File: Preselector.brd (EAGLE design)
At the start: 183 x 123.8 mm, 167 parts, among them IC4 TPS7A8101DRB, IC58 LMZ31707RVQ, Q2 FDV303N, X1 0733660061, X10 0733660061, X11 0733660061, X12 0733660061, X13 0733660061, X14 0733660061, X15 0733660061, X16 0733660061, X17 0733660061, X18 0733660061, X19 0733660061, X2 0733660061, X20 0733660061, X21 0733660061, X22 0733660061, X23 0733660061, X24 0733660061, X25 0733660061, X26 0733660061, X27 0733660061, X28 0733660061, X29 0733660061, X3 0733660061, X30 0733660061, X31 0733660061, X32 0733660061, X4 0733660061, X5 0733660061, X6 0733660061, X7 0733660061, X8 0733660061, X9 0733660061

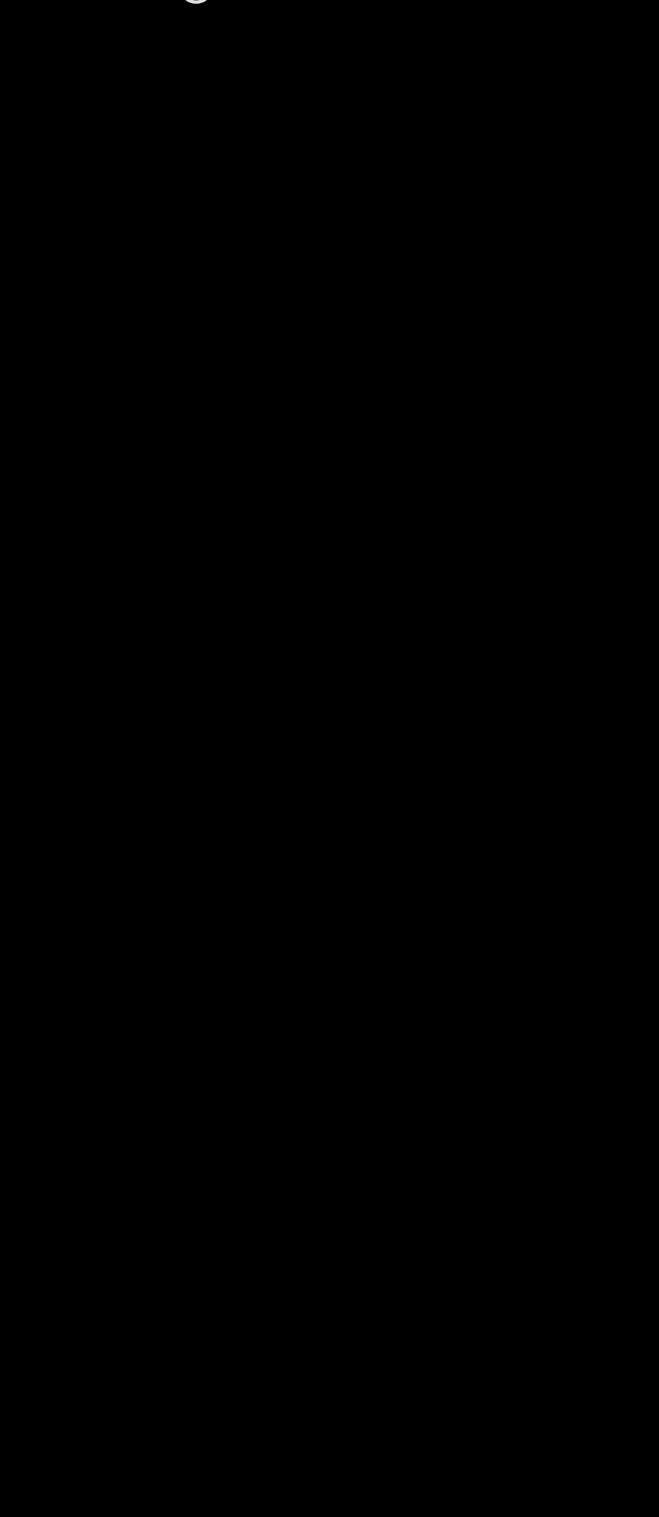
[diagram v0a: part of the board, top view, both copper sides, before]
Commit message: Added first 2 LDO's on 2m band
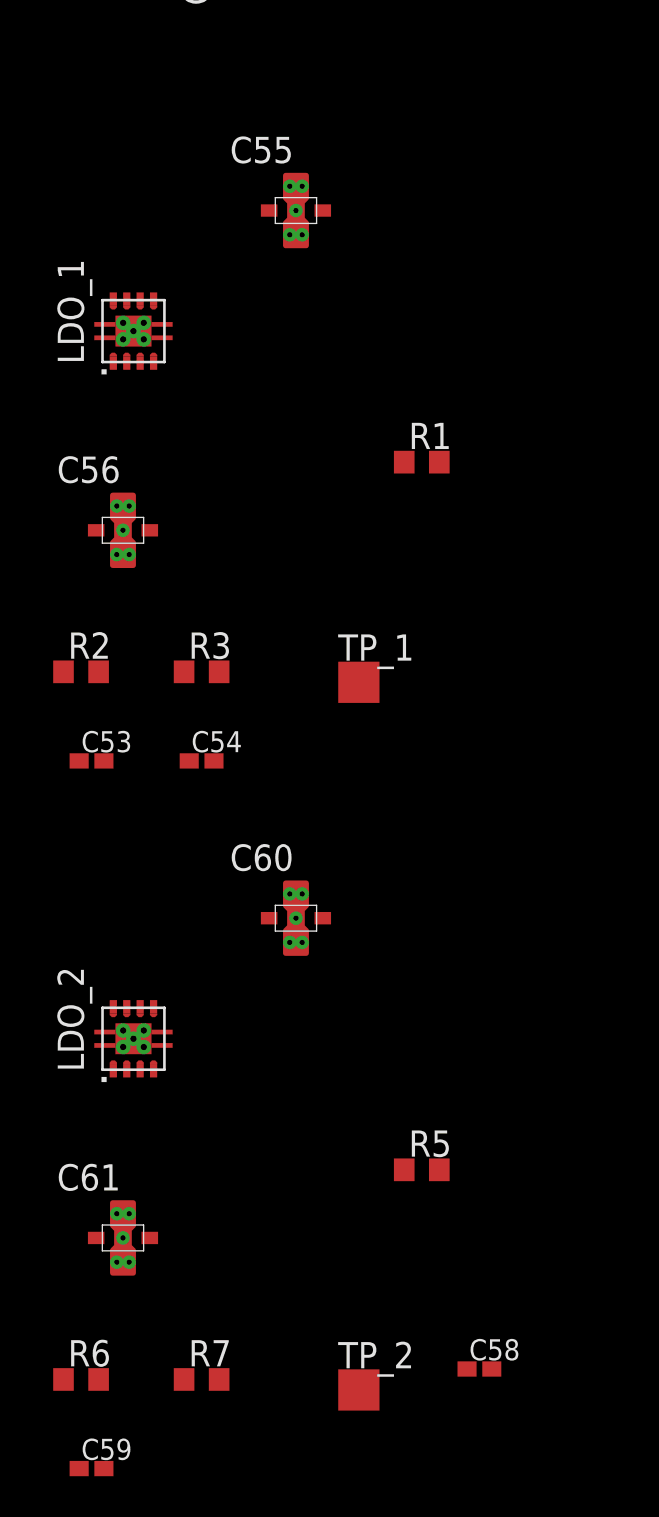
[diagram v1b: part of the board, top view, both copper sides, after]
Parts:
- added C53, C54, C58, C59: 470n, rcl:C0402K
- added C55, C56, C60, C61: NFM21PS106B0J3D, DEEP EDDY:NFM21PS
- added LDO_1, LDO_2: TPS7A8101DRB, DEEP EDDY:DRB
- added R1, R3, R5, R7: 10.0k, rcl:R0603
- added R2, R6: 52.3k, rcl:R0603
- added TP_1, TP_2: TPTP20SQ, testpad:TP20SQ
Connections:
- new net LDO_1_5V: C2.1, C3.1, C54.2, C56.OUT, L1.2, R2.1, TP_1.TP
- new net LDO_1_5V1: C59.2, C61.OUT, R6.1, TP_2.TP
- new net N$12: C54.1, LDO_1.3, R2.2, R3.1
- new net N$13: C53.1, LDO_1.6
- new net N$14: C55.OUT, LDO_1.7, LDO_1.8
- new net N$15: C56.IN, LDO_1.1, LDO_1.2
- new net N$16: C59.1, LDO_2.3, R6.2, R7.1
- new net N$17: C58.1, LDO_2.6
- new net N$18: C60.OUT, LDO_2.7, LDO_2.8
- new net N$19: C61.IN, LDO_2.1, LDO_2.2
- net +5V0: no longer C2.1, C3.1, L1.2
- net +5V3: now also C55.IN, C60.IN, R1.1, R5.1
- net GND: now also C53.2, C55.GND1, C55.GND2, C55.GND3, C55.GND4, C55.GND5, C55.GND6, C55.GND7, C55.GND8, C56.GND1, C56.GND2, C56.GND3, C56.GND4, C56.GND5, C56.GND6, C56.GND7, C56.GND8, C58.2, C60.GND1, C60.GND2, C60.GND3, C60.GND4, C60.GND5, C60.GND6, C60.GND7, C60.GND8, C61.GND1, C61.GND2, C61.GND3, C61.GND4, C61.GND5, C61.GND6, C61.GND7, C61.GND8, LDO_1.4, LDO_1.P1, LDO_1.P2, LDO_1.P3, LDO_1.P4, LDO_1.P5, LDO_1.PAD, LDO_2.4, LDO_2.P1, LDO_2.P2, LDO_2.P3, LDO_2.P4, LDO_2.P5, LDO_2.PAD, R3.2, R7.2
- net PRE_PWR: now also LDO_1.5, LDO_2.5, R1.2, R5.2

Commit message: I think i did it correctly.
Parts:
- moved C28 2.93 mm to (19.7, 95.2)
- moved C27 2.93 mm to (17.8, 95.2)
- moved C35 2.80 mm to (89.0, 95.1)
- moved C36 2.80 mm to (90.9, 95.1)
- moved C31 2.54 mm to (53.5, 94.9)
- moved C32 2.54 mm to (55.4, 94.9)
- moved C23 2.54 mm to (97.4, 76.7)
- moved C24 2.54 mm to (99.3, 76.7)
- moved C19 2.43 mm to (57.8, 76.6)
- moved C20 2.43 mm to (59.7, 76.6)
- moved C15 2.32 mm to (17.7, 77.5)
- moved C16 2.32 mm to (19.6, 77.5)
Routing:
- added copper zone on layer 1, net N$20
- added copper zone on layer 1, net N$22

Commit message: Added LDO's to schematic, will add to board shortly.
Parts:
- added C100, C101, C62, C63, C66, C67, C70, C71, C76, C77, C80, C81, C84, C85, C88, C89, C92, C93, C96, C97: 470n, rcl:C0402K
- added C102, C103, C64, C65, C68, C69, C74, C75, C78, C79, C82, C83, C86, C87, C90, C91, C94, C95, C98, C99: NFM21PS106B0J3D, DEEP EDDY:NFM21PS
- added LDO_10, LDO_11, LDO_12, LDO_3, LDO_4, LDO_5, LDO_6, LDO_7, LDO_8, LDO_9: TPS7A8101DRB, DEEP EDDY:DRB
- added R10, R11, R14, R15, R19, R21, R23, R24, R26, R27, R29, R30, R32, R33, R35, R36, R38, R39, R41, R8: 10.0k, rcl:R0603
- added R12, R16, R22, R25, R28, R31, R34, R37, R40, R9: 52.3k, rcl:R0603
- added TP_10, TP_11, TP_12, TP_3, TP_4, TP_5, TP_6, TP_7, TP_8, TP_9: TPTP20SQ, testpad:TP20SQ
- moved R20 58.6 mm to (-119.4, -63.0), turned to 270 degrees
- moved +5V14 54.4 mm to (-114.5, -63.9), turned to 0 degrees
- moved C72 50.1 mm to (-116.5, -59.9), turned to 270 degrees
- moved C73 46.7 mm to (-113.7, -59.8), turned to 270 degrees
- moved R18 45.5 mm to (-108.6, -61.7), turned to 270 degrees
- moved R17 43.9 mm to (-111.2, -59.7), turned to 90 degrees
- moved IC4 43.3 mm to (-115.8, -55.9), turned to 0 degrees
- moved C52 39.1 mm to (-116.5, -52.0), turned to 270 degrees
- moved C57 37.8 mm to (-113.1, -54.7), turned to 270 degrees
- moved C15 1.14 mm to (17.1, 78.5), turned to 90 degrees
- moved C16 1.14 mm to (19.1, 78.5)
- moved C19 1.05 mm to (57.5, 77.6), turned to 90 degrees
- moved C20 1.05 mm to (59.4, 77.6), turned to 90 degrees
- moved C23 0.81 mm to (96.9, 77.3), turned to 90 degrees
- moved C32 0.81 mm to (54.9, 95.5), turned to 90 degrees
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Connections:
- removed net +5V0: C10.1, C11.1, C15.1, C16.1, C19.1, C20.1, C23.1, C24.1, C27.1, C28.1, C31.1, C32.1, C35.1, C36.1, C40.1, C41.1, C44.1, C45.1, C48.1, C49.1, C6.1, C7.1, L10.2, L11.2, L12.1, L13.2, L14.2, L15.2, L18.2, L21.2, L24.2, L4.2, L7.1
- removed net LDO_1_5V1: C59.2, C61.OUT, R6.1, TP_2.TP
- new net LDO_10_5V: C40.1, C41.1, C93.2, C95.OUT, L18.2, R34.1, TP_10.TP
- new net LDO_11_5V: C44.1, C45.1, C97.2, C99.OUT, L21.2, R37.1, TP_11.TP
- new net LDO_12_5V: C101.2, C103.OUT, C48.1, C49.1, L24.2, R40.1, TP_12.TP
- new net LDO_2_5V: C59.2, C6.1, C61.OUT, C7.1, L4.2, R6.1, TP_2.TP
- new net LDO_3_5V: C10.1, C11.1, C63.2, C65.OUT, L7.1, R9.1, TP_3.TP
- new net LDO_4_5V: C15.1, C16.1, C67.2, C69.OUT, L10.2, R12.1, TP_4.TP
- new net LDO_5_5V: C19.1, C20.1, C71.2, C75.OUT, L11.2, R16.1, TP_5.TP
- new net LDO_6_5V: C23.1, C24.1, C77.2, C79.OUT, L12.1, R22.1, TP_6.TP
- new net LDO_7_5V: C27.1, C28.1, C81.2, C83.OUT, L13.2, R25.1, TP_7.TP
- new net LDO_8_5V: C31.1, C32.1, C85.2, C87.OUT, L14.2, R28.1, TP_8.TP
- new net LDO_9_5V: C35.1, C36.1, C89.2, C91.OUT, L15.2, R31.1, TP_9.TP
- new net N$20: C63.1, LDO_3.3, R10.1, R9.2
- new net N$22: C62.1, LDO_3.6
- new net N$24: C64.OUT, LDO_3.7, LDO_3.8
- new net N$25: C65.IN, LDO_3.1, LDO_3.2
- new net N$27: C67.1, LDO_4.3, R12.2, R14.1
- new net N$28: C66.1, LDO_4.6
- new net N$30: C68.OUT, LDO_4.7, LDO_4.8
- new net N$33: C69.IN, LDO_4.1, LDO_4.2
- new net N$34: C71.1, LDO_5.3, R16.2, R19.1
- new net N$36: C70.1, LDO_5.6
- new net N$38: C74.OUT, LDO_5.7, LDO_5.8
- new net N$39: C75.IN, LDO_5.1, LDO_5.2
- new net N$40: C81.1, LDO_7.3, R25.2, R26.1
- new net N$41: C77.1, LDO_6.3, R22.2, R23.1
- new net N$42: C76.1, LDO_6.6
- new net N$43: C78.OUT, LDO_6.7, LDO_6.8
- new net N$45: C79.IN, LDO_6.1, LDO_6.2
- new net N$46: C80.1, LDO_7.6
- new net N$47: C82.OUT, LDO_7.7, LDO_7.8
- new net N$48: C83.IN, LDO_7.1, LDO_7.2
- new net N$49: C85.1, LDO_8.3, R28.2, R29.1
- new net N$50: C84.1, LDO_8.6
- new net N$51: C86.OUT, LDO_8.7, LDO_8.8
- new net N$52: C87.IN, LDO_8.1, LDO_8.2
- new net N$53: C89.1, LDO_9.3, R31.2, R32.1
- new net N$54: C88.1, LDO_9.6
- new net N$56: C90.OUT, LDO_9.7, LDO_9.8
- new net N$57: C91.IN, LDO_9.1, LDO_9.2
- new net N$61: C93.1, LDO_10.3, R34.2, R35.1
- new net N$62: C92.1, LDO_10.6
- new net N$63: C94.OUT, LDO_10.7, LDO_10.8
- new net N$64: C95.IN, LDO_10.1, LDO_10.2
- new net N$66: C97.1, LDO_11.3, R37.2, R38.1
- new net N$67: C96.1, LDO_11.6
- new net N$68: C98.OUT, LDO_11.7, LDO_11.8
- new net N$69: C99.IN, LDO_11.1, LDO_11.2
- new net N$70: C101.1, LDO_12.3, R40.2, R41.1
- new net N$71: C100.1, LDO_12.6
- new net N$72: C102.OUT, LDO_12.7, LDO_12.8
- new net N$73: C103.IN, LDO_12.1, LDO_12.2
- net +5V3: now also C102.IN, C64.IN, C68.IN, C74.IN, C78.IN, C82.IN, C86.IN, C90.IN, C94.IN, C98.IN, R11.1, R15.1, R21.1, R24.1, R27.1, R30.1, R33.1, R36.1, R39.1, R8.1
- net GND: now also C100.2, C102.GND1, C102.GND2, C102.GND3, C102.GND4, C102.GND5, C102.GND6, C102.GND7, C102.GND8, C103.GND1, C103.GND2, C103.GND3, C103.GND4, C103.GND5, C103.GND6, C103.GND7, C103.GND8, C62.2, C64.GND1, C64.GND2, C64.GND3, C64.GND4, C64.GND5, C64.GND6, C64.GND7, C64.GND8, C65.GND1, C65.GND2, C65.GND3, C65.GND4, C65.GND5, C65.GND6, C65.GND7, C65.GND8, C66.2, C68.GND1, C68.GND2, C68.GND3, C68.GND4, C68.GND5, C68.GND6, C68.GND7, C68.GND8, C69.GND1, C69.GND2, C69.GND3, C69.GND4, C69.GND5, C69.GND6, C69.GND7, C69.GND8, C70.2, C74.GND1, C74.GND2, C74.GND3, C74.GND4, C74.GND5, C74.GND6, C74.GND7, C74.GND8, C75.GND1, C75.GND2, C75.GND3, C75.GND4, C75.GND5, C75.GND6, C75.GND7, C75.GND8, C76.2, C78.GND1, C78.GND2, C78.GND3, C78.GND4, C78.GND5, C78.GND6, C78.GND7, C78.GND8, C79.GND1, C79.GND2, C79.GND3, C79.GND4, C79.GND5, C79.GND6, C79.GND7, C79.GND8, C80.2, C82.GND1, C82.GND2, C82.GND3, C82.GND4, C82.GND5, C82.GND6, C82.GND7, C82.GND8, C83.GND1, C83.GND2, C83.GND3, C83.GND4, C83.GND5, C83.GND6, C83.GND7, C83.GND8, C84.2, C86.GND1, C86.GND2, C86.GND3, C86.GND4, C86.GND5, C86.GND6, C86.GND7, C86.GND8, C87.GND1, C87.GND2, C87.GND3, C87.GND4, C87.GND5, C87.GND6, C87.GND7, C87.GND8, C88.2, C90.GND1, C90.GND2, C90.GND3, C90.GND4, C90.GND5, C90.GND6, C90.GND7, C90.GND8, C91.GND1, C91.GND2, C91.GND3, C91.GND4, C91.GND5, C91.GND6, C91.GND7, C91.GND8, C92.2, C94.GND1, C94.GND2, C94.GND3, C94.GND4, C94.GND5, C94.GND6, C94.GND7, C94.GND8, C95.GND1, C95.GND2, C95.GND3, C95.GND4, C95.GND5, C95.GND6, C95.GND7, C95.GND8, C96.2, C98.GND1, C98.GND2, C98.GND3, C98.GND4, C98.GND5, C98.GND6, C98.GND7, C98.GND8, C99.GND1, C99.GND2, C99.GND3, C99.GND4, C99.GND5, C99.GND6, C99.GND7, C99.GND8, LDO_10.4, LDO_10.P1, LDO_10.P2, LDO_10.P3, LDO_10.P4, LDO_10.P5, LDO_10.PAD, LDO_11.4, LDO_11.P1, LDO_11.P2, LDO_11.P3, LDO_11.P4, LDO_11.P5, LDO_11.PAD, LDO_12.4, LDO_12.P1, LDO_12.P2, LDO_12.P3, LDO_12.P4, LDO_12.P5, LDO_12.PAD, LDO_3.4, LDO_3.P1, LDO_3.P2, LDO_3.P3, LDO_3.P4, LDO_3.P5, LDO_3.PAD, LDO_4.4, LDO_4.P1, LDO_4.P2, LDO_4.P3, LDO_4.P4, LDO_4.P5, LDO_4.PAD, LDO_5.4, LDO_5.P1, LDO_5.P2, LDO_5.P3, LDO_5.P4, LDO_5.P5, LDO_5.PAD, LDO_6.4, LDO_6.P1, LDO_6.P2, LDO_6.P3, LDO_6.P4, LDO_6.P5, LDO_6.PAD, LDO_7.4, LDO_7.P1, LDO_7.P2, LDO_7.P3, LDO_7.P4, LDO_7.P5, LDO_7.PAD, LDO_8.4, LDO_8.P1, LDO_8.P2, LDO_8.P3, LDO_8.P4, LDO_8.P5, LDO_8.PAD, LDO_9.4, LDO_9.P1, LDO_9.P2, LDO_9.P3, LDO_9.P4, LDO_9.P5, LDO_9.PAD, R10.2, R14.2, R19.2, R23.2, R26.2, R29.2, R32.2, R35.2, R38.2, R41.2
- net PRE_PWR: now also LDO_10.5, LDO_11.5, LDO_12.5, LDO_3.5, LDO_4.5, LDO_5.5, LDO_6.5, LDO_7.5, LDO_8.5, LDO_9.5, R11.2, R15.2, R21.2, R24.2, R27.2, R30.2, R33.2, R36.2, R39.2, R8.2
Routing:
- net SAW_1_OUT: track 17.9 -> 16.3 mm
- net LNA_12_OUT: track 10.7 -> 9.29 mm
- removed copper zone on layer 1, net D'GND
- removed copper zone on layer 1, net N$20
- removed copper zone on layer 1, net N$22
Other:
- board text removed: "This ground needs to be up like the 4m and 2m for all these style caps. Via should be 3 grid spaces away at 10mil, if no room then 2 is fine."

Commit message: hi kenneth, just pushing the files that I worked on in class
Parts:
- moved +5V14 168.7 mm to (-114.5, -232.5)
- moved C52 168.7 mm to (-116.5, -220.6)
- moved C57 168.7 mm to (-113.1, -223.3)
- moved C72 168.7 mm to (-116.5, -228.5)
- moved C73 168.7 mm to (-113.7, -228.5)
- moved IC4 168.7 mm to (-115.8, -224.5)
- moved R17 168.7 mm to (-111.2, -228.3)
- moved R18 168.7 mm to (-108.6, -230.4)
- moved R20 168.7 mm to (-119.4, -231.7)
- moved R11 28.5 mm to (-104.1, -165.6), turned to 270 degrees
- moved C66 26.0 mm to (-98.3, -157.0), turned to 270 degrees
- moved R5 25.9 mm to (-101.9, -95.5), turned to 270 degrees
- moved C70 24.3 mm to (-93.5, -186.2), turned to 270 degrees
- moved C58 24.0 mm to (-95.5, -87.1), turned to 270 degrees
- moved R15 22.8 mm to (-99.6, -194.6), turned to 270 degrees
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
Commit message: Oriented a few more LDO's and placed one on the board to see what it looked like.
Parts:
- moved C81 395.2 mm to (26.7, 102.4), turned to 180 degrees
- moved R25 388.2 mm to (26.2, 99.3)
- moved TP_7 387.3 mm to (22.9, 102.9), turned to 270 degrees
- moved C83 387.0 mm to (26.7, 105.4), turned to 180 degrees
- moved C80 386.2 mm to (32.0, 101.9), turned to 180 degrees
- moved R26 383.2 mm to (24.1, 96.5), turned to 180 degrees
- moved R24 381.7 mm to (23.4, 108.5), turned to 180 degrees
- moved LDO_7 378.6 mm to (31.0, 104.9), turned to 270 degrees
- moved C82 372.3 mm to (35.3, 105.3), turned to 180 degrees
- moved R18 99.6 mm to (-106.0, -329.9)
- moved +5V14 99.6 mm to (-111.9, -332.1)
- moved C52 99.6 mm to (-113.9, -320.2)
- moved R20 99.6 mm to (-116.8, -331.2)
- moved C57 99.6 mm to (-110.5, -322.9)
- moved C72 99.6 mm to (-113.9, -328.1)
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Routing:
- net LDO_7_5V: track 0.00 -> 43.5 mm
- net N$40: track 0.00 -> 11.5 mm
- net N$46: track 0.00 -> 3.99 mm
- net N$47: track 0.00 -> 2.75 mm
- net N$48: track 0.00 -> 2.47 mm

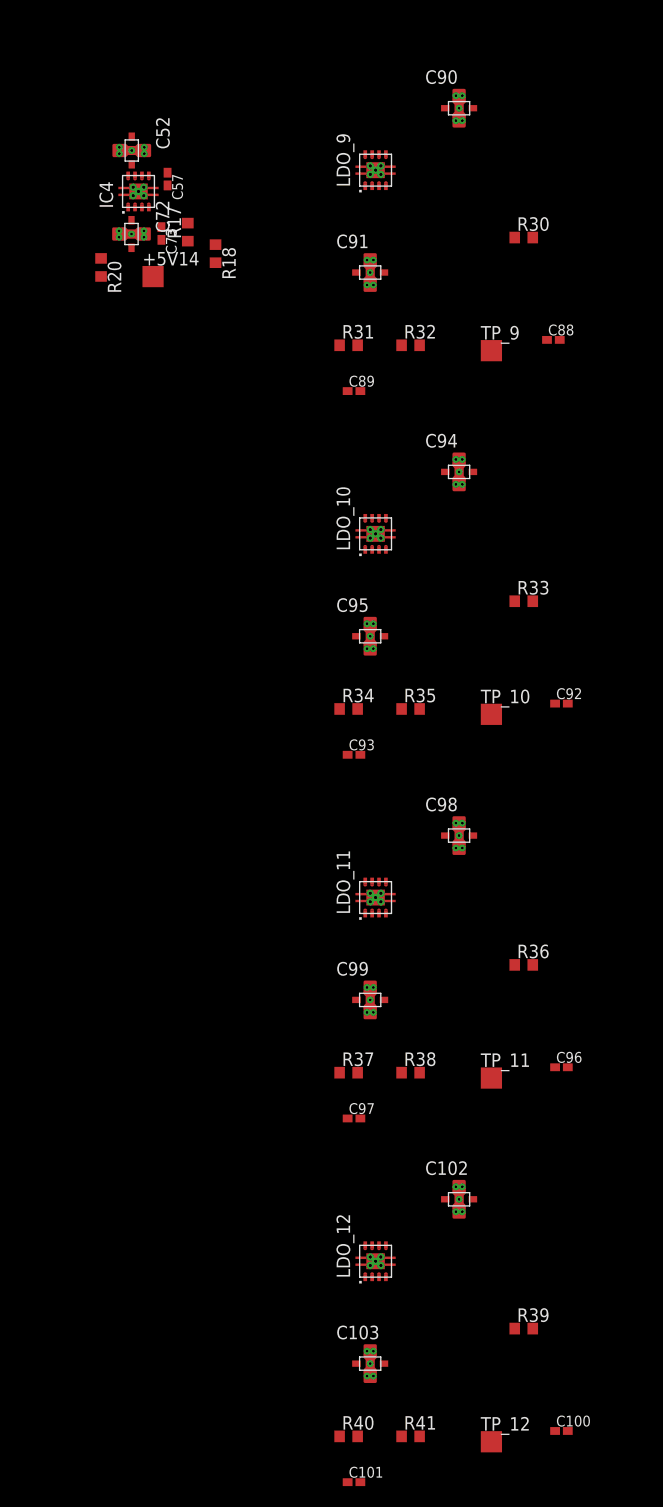
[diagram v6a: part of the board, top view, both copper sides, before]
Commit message: Finished modeling the LDO configurations
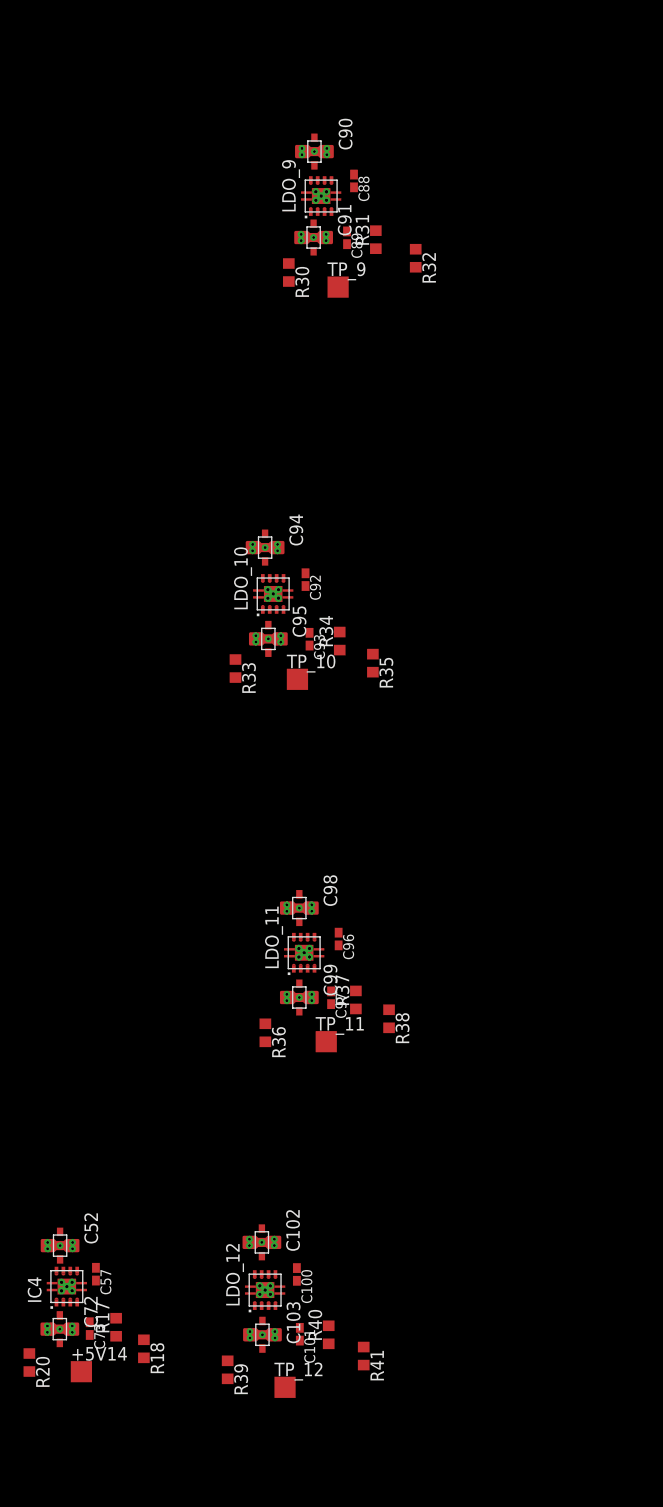
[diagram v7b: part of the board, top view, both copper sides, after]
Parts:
- moved C57 103.5 mm to (-117.3, -426.2)
- moved C72 103.5 mm to (-120.7, -431.3)
- moved IC4 103.5 mm to (-120.0, -427.3)
- moved R17 103.5 mm to (-115.4, -431.2)
- moved +5V14 103.5 mm to (-118.7, -435.4)
- moved C52 103.5 mm to (-120.7, -423.5)
- moved C73 103.5 mm to (-117.9, -431.3)
- moved R18 103.5 mm to (-112.8, -433.2)
- moved R20 103.5 mm to (-123.6, -434.5)
- moved C100 29.0 mm to (-98.3, -426.2), turned to 270 degrees
- moved R39 28.2 mm to (-104.9, -435.2), turned to 270 degrees
- moved R33 27.9 mm to (-104.1, -369.1), turned to 270 degrees
- moved C92 26.8 mm to (-97.5, -360.7), turned to 270 degrees
- moved R36 25.2 mm to (-101.3, -403.4), turned to 270 degrees
- moved C96 24.2 mm to (-94.4, -394.6), turned to 270 degrees
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
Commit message: Hey, Kenneth, I added the LDO's and routed the ones on the 2m band, let me know if that looks right so I can continue working on it as is. Thanks.
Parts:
- moved R39 521.4 mm to (130.2, 30.3), turned to 180 degrees
- moved C103 515.6 mm to (133.5, 27.0), turned to 180 degrees
- moved TP_12 514.9 mm to (128.6, 24.8), turned to 270 degrees
- moved LDO_12 513.4 mm to (137.7, 26.7), turned to 270 degrees
- moved C102 512.0 mm to (142.2, 27.0), turned to 180 degrees
- moved C101 510.8 mm to (133.6, 23.4), turned to 180 degrees
- moved C100 508.8 mm to (139.2, 23.7), turned to 180 degrees
- moved R40 507.2 mm to (133.5, 20.7), turned to 0 degrees
- moved R41 503.6 mm to (131.5, 17.4), turned to 180 degrees
- moved R30 492.2 mm to (93.3, 121.3), turned to 180 degrees
- moved C91 487.2 mm to (96.6, 118.7), turned to 180 degrees
- moved TP_9 486.9 mm to (93.1, 116.2), turned to 270 degrees
- moved LDO_9 484.2 mm to (101.0, 117.8), turned to 270 degrees
- moved C89 483.0 mm to (97.1, 115.3), turned to 180 degrees
- moved C90 482.8 mm to (105.5, 118.2), turned to 180 degrees
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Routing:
- net LDO_9_5V: track 0.00 -> 44.1 mm
- net LDO_8_5V: track 0.00 -> 43.6 mm
- net N$53: track 0.00 -> 11.8 mm
- net N$49: track 0.00 -> 11.2 mm
- net N$50: track 0.00 -> 4.12 mm
- net N$54: track 0.00 -> 4.04 mm
- net N$56: track 0.00 -> 3.73 mm
- net N$57: track 0.00 -> 2.90 mm
- net N$51: track 0.00 -> 2.90 mm
- net N$52: track 0.00 -> 2.70 mm
